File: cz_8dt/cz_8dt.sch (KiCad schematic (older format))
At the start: 638 parts, among them IC1001 74LS09, IC1002 4001, IC1003 4049, IC101 MC4044, IC102 CD4053B, IC103 HD440072, IC104 4069, IC105 HA11720, IC106 74LS221, IC1101 74LS145, IC1102 74LS145, IC1103 74LS145, IC1104 7406, IC1105 74LS26, IC1106 7408, IC1201 7407, IC1202 7406, IC1203 74LS74, IC301 TA7348P, IC302 TA7348P, IC303 TA7347P, IC305 TA7348P, IC401 TA7348P, IC402 TA7348P, IC403 TA7347P, IC404 BA7001, IC404 TA7347P, IC601 X0065CE, IC602 74LS221, IC603 74LS221, IC604 74LS221, IC801 TA7608CP, IC901 74159, IC902 74LS126, IC903 74LS126, IC904 74279, IC905 74279, IC906 74279, IC907 74LS126, IC908 74LS11, IC909 7406, Q1001 Q_NPN_BCE, Q1002 Q_NPN_BCE, Q101 Q_NPN_BCE, Q102 Q_NPN_BCE, Q103 Q_NPN_BCE, Q104 Q_NPN_BCE, Q105 Q_NPN_BCE, Q106 Q_NPN_BCE, Q107 Q_NPN_BCE, Q108 Q_NPN_BCE, Q109 Q_NPN_BCE, Q1099 Q_NPN_BCE, Q1101 Q_PNP_BCE, Q1102 Q_NPN_BCE, Q1103 Q_NPN_BCE, Q1104 Q_PNP_BCE, Q1105 Q_NPN_BCE, Q1106 Q_NPN_BCE, Q1107 Q_PNP_BCE, Q1108 Q_NPN_BCE, Q1109 Q_NPN_BCE, Q1110 Q_NPN_BCE, Q1111 Q_NPN_BCE, Q1112 Q_NPN_BCE, Q1113 Q_NPN_BCE, Q1114 Q_NPN_BCE, Q1115 Q_NPN_BCE, Q112 Q_NPN_BCE, Q301 Q_NPN_BCE, Q303 Q_NPN_BCE, Q304 Q_NPN_BCE, Q316 Q_NPN_BCE, Q401 Q_NPN_BCE, Q402 Q_PNP_BCE, Q403 Q_NPN_BCE, Q413 Q_NPN_BCE, Q414 Q_NPN_BCE, Q415 Q_NPN_BCE, Q416 Q_NPN_BCE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

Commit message: transistor types added and corrections...
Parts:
- removed Q1112, Q1113, Q1114, Q413, Q?: Q_NPN_BCE, symbol Device:Q_NPN_BCE
- added Q111: A105, symbol Device:Q_PNP_BCE
- added Q1112, Q1113, Q1114, Q413: A1015, symbol Device:Q_PNP_BCE
- Q1001, Q1002, Q101, Q102, Q103, Q105, Q109, Q1099, Q1102, Q1103, Q1105, Q1106, Q1108, Q1109, Q1110, Q1111, Q1115, Q112, Q301, Q303, Q304, Q316, Q401, Q403, Q414, Q415, Q416, Q601, Q602, Q603, Q604, Q605: value Q_NPN_BCE -> C1815
- Q104, Q107: value Q_NPN_BCE -> C460
- Q106, Q108: value Q_NPN_BCE -> A454
- Q1101, Q1104, Q1107, Q402: value Q_PNP_BCE -> A1015
- Q412: renamed from Q?; value Q_NPN_BCE -> C1815
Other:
- moved on the sheet: C419, C420, C421, C438, C439, C440, C601, C602, C603, C604, C606, C607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

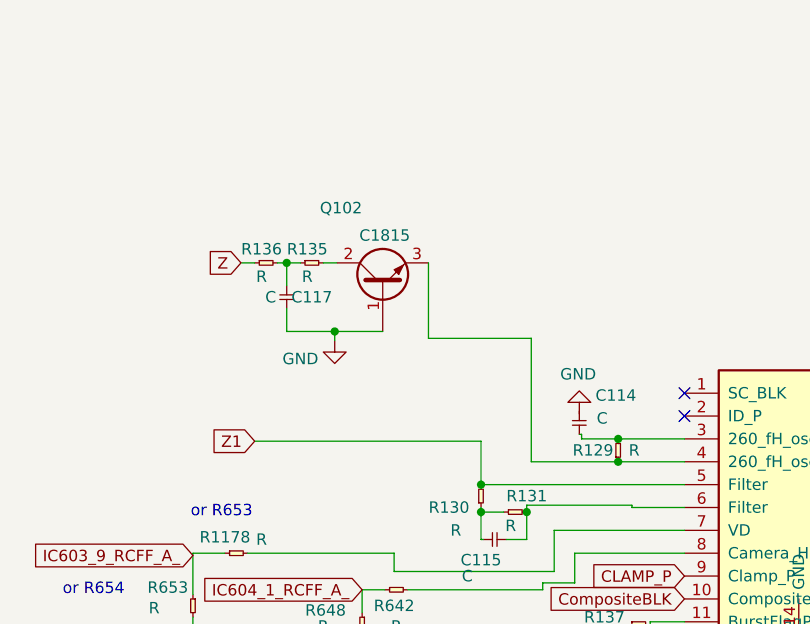
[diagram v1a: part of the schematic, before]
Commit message: changed Q102 to D102 (1SV55 type)
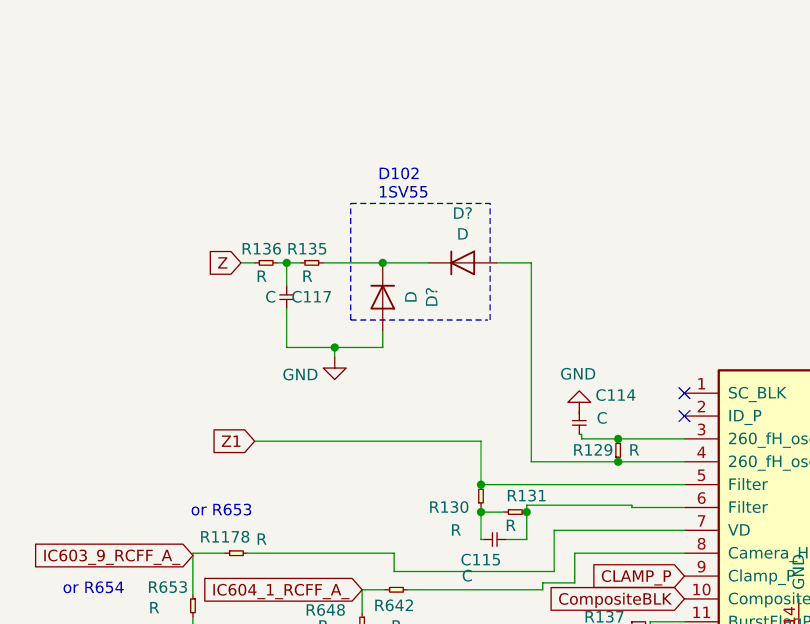
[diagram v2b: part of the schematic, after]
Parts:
- removed Q102: C1815, symbol Device:Q_NPN_BCE
- added D? (x2): D, symbol Device:D
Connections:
- wire segments 2462 -> 2463
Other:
- note added: "D102\n1SV55"
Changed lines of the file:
@@
 L power:GND #PWR?
 U 1 1 668AD11E
-P 15450 6290
-F 0 "#PWR?" H 15450 6040 50  0001 C CNN
-F 1 "GND" H 15300 6210 50  0000 C CNN
-F 2 "" H 15450 6290 50  0001 C CNN
-F 3 "" H 15450 6290 50  0001 C CNN
-	1    15450 6290
+P 15450 6360
+F 0 "#PWR?" H 15450 6110 50  0001 C CNN
+F 1 "GND" H 15300 6280 50  0000 C CNN
+F 2 "" H 15450 6360 50  0001 C CNN
+F 3 "" H 15450 6360 50  0001 C CNN
+	1    15450 6360
 	1    0    0    -1
 $EndComp
@@
 	15100 5950 15040 5950
 Wire Wire Line
-	15400 5950 15460 5950
-$Comp
-L Device:Q_NPN_BCE Q102
-U 1 1 66C5C3E9
-P 15660 6050
-F 0 "Q102" V 16000 6140 50  0000 L CNN
-F 1 "C1815" V 15880 5930 50  0000 L CNN
-F 2 "" H 15860 6150 50  0001 C CNN
-F 3 "~" H 15660 6050 50  0001 C CNN
-	1    15660 6050
-	0    -1   -1   0
-$EndComp
-Wire Wire Line
-	15660 6250 15450 6250
-Wire Wire Line
-	15450 6250 15450 6290
-Wire Wire Line
-	15450 6250 15240 6250
-Wire Wire Line
-	15240 6250 15240 6150
-Connection ~ 15450 6250
+	15450 6320 15450 6360
 Text GLabel 15100 6730 0    50   Input ~ 0
 Z1
@@
 Connection ~ 16290 7040
 Wire Wire Line
-	15860 6280 15860 5950
-Wire Wire Line
-	15860 6280 16310 6280
-Wire Wire Line
 	16750 7010 16750 7020
 Wire Wire Line
@@
 Wire Wire Line
 	16690 6820 16310 6820
-Wire Wire Line
-	16310 6820 16310 6280
 Connection ~ 16690 6820
 Wire Wire Line
@@
 Wire Wire Line
 	16520 16860 16690 16860
+$Comp
+L Device:D D?
+U 1 1 E546E3F8
+P 16010 5950
+F 0 "D?" H 16010 6166 50  0000 C CNN
+F 1 "D" H 16010 6075 50  0000 C CNN
+F 2 "" H 16010 5950 50  0001 C CNN
+F 3 "~" H 16010 5950 50  0001 C CNN
+	1    16010 5950
+	1    0    0    -1
+$EndComp
+$Comp
+L Device:D D?
+U 1 1 E546F3CA
+P 15660 6100
+F 0 "D?" H 15660 6316 50  0000 C CNN
+F 1 "D" H 15660 6225 50  0000 C CNN
+F 2 "" H 15660 6100 50  0001 C CNN
+F 3 "~" H 15660 6100 50  0001 C CNN
+	1    15660 6100
+	0    1    1    0
+$EndComp
+Wire Wire Line
+	15400 5950 15660 5950
+Wire Wire Line
+	15660 5950 15860 5950
+Connection ~ 15660 5950
+Wire Wire Line
+	16160 5950 16310 5950
+Wire Wire Line
+	16310 5950 16310 6820
+Wire Notes Line
+	15520 6200 16120 6200
+Text Notes 15640 5680 0    50   ~ 0
+D102\n1SV55
+Wire Wire Line
+	15660 6250 15660 6320
+Wire Wire Line
+	15660 6320 15450 6320
+Wire Wire Line
+	15450 6320 15240 6320
+Connection ~ 15450 6320
+Wire Wire Line
+	15240 6150 15240 6320
+Wire Notes Line
+	15520 6200 15520 5690
+Wire Notes Line
+	15520 5690 16130 5690
+Wire Notes Line
+	16130 6200 16130 5690
 $EndSCHEMATC

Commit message: updated capa/resistor lists. Added J1/J2/K1/K2
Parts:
- added C342: 100uf/16v, symbol agg-kicad:CP
- added C343, C344, C345: 10uf/16v, symbol agg-kicad:CP
- added C?: 100uf/35V, symbol agg-kicad:CP
- added D303, D305, D306, D307, D308, D309, D310: D, symbol agg-kicad:D
- added D304: 4.7R, symbol agg-kicad:R
- added Q305: A1015, symbol Device:Q_PNP_BCE
- added Q306, Q307, Q308, Q309, Q310, Q311, Q901: C1815, symbol Device:Q_NPN_BCE
- added R1164, R177: R_POT, symbol Device:R_POT
- added R1199, R360: R, symbol agg-kicad:R
- added R358: 10K, symbol agg-kicad:R
- added R359, R361, R363, R365: 3.3K, symbol agg-kicad:R
- added R362, R364, R366: 1K, symbol agg-kicad:R
- added R940: 27R, symbol agg-kicad:R
- added R941: 68R, symbol agg-kicad:R
- added R942: 220R, symbol agg-kicad:R
- added R?: 82R, symbol agg-kicad:R
- renumbered Q1110 to Q110
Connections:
- net labels added: 15V???, RGB21_AUDIO_OUT_L, RGB21_AUDIO_OUT_R, YM_IN, YM_OUT
- wire segments 2463 -> 2557
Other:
- note added: "Audio dc level board ??? (F2868CE)\n\n"
- note added: "COMP video"
- note added: "I-connector:\n------------\nV-position\nH-position\nColor Intensity\nColor tone\nVideo adjustment"
- note added: "Shadow"

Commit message: added power supply schematics
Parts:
- added A: CONN_01x02, symbol agg-kicad:CONN_01x02
- added B: CONN_01x03, symbol agg-kicad:CONN_01x03
- added C701: 104K, symbol agg-kicad:C
- added C702, C703: 103 / 250v, symbol agg-kicad:C
- added C704, C708, C712: 103K, symbol agg-kicad:C
- added C705: 2200uf/35v, symbol agg-kicad:CP
- added C706: 47uf/25v, symbol agg-kicad:CP
- added C707: 100uf/16v, symbol agg-kicad:CP
- added C709: 2200uf/25v, symbol agg-kicad:CP
- added C710: 47uf/16v, symbol agg-kicad:CP
- added C?: 2200uf? 35v ?, symbol agg-kicad:CP
- added D701, D702: D, symbol agg-kicad:D
- added D703: ZENER, symbol agg-kicad:ZENER
- added E: CONN_01x04, symbol agg-kicad:CONN_01x04
- added F701: FUSE, symbol agg-kicad:FUSE
- added IC: L7812, symbol Regulator_Linear:L7812
- added IC702: LM7805, Package_TO_SOT_THT:TO-220-3_Vertical, symbol Regulator_Linear:LM7805_TO220
- added L701: _, symbol Device:Transformer_1P_1S
- added R701: =wire, symbol agg-kicad:R
- added R702: 0.56R, symbol agg-kicad:R
- added R703: 18R, symbol agg-kicad:R
- added R?: 33R-5W, symbol agg-kicad:R
- added R?: 0.5R, symbol agg-kicad:R
- added SW?: SWITCH_SPST, symbol agg-kicad:SWITCH_SPST
- added T?: Transformer_1P_1S, symbol Device:Transformer_1P_1S
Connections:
- net labels added: 15V, AC_100V_1, AC_100V_2, E1, E2, E3, E4
- net labels removed: 15V???
- wire segments 2557 -> 2677
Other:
- note added: "12V\n7.2V\n5V\nGND"
- note added: "<--red wire"
- note added: "Joystick port\nfor external control"
- note added: "POWER SUPPLY"
- note added: "black"
- note added: "black wire ->"
- note added: "brown"
- note added: "brown\n wire\n<--\n"
- note added: "orange"
- note added: "red"
- note added: "to Power\n LED"
- note added: "yellow"
- moved on the sheet: C628, IC1003C, IC1106D, IC901, R916, R917, R918, R919, R924

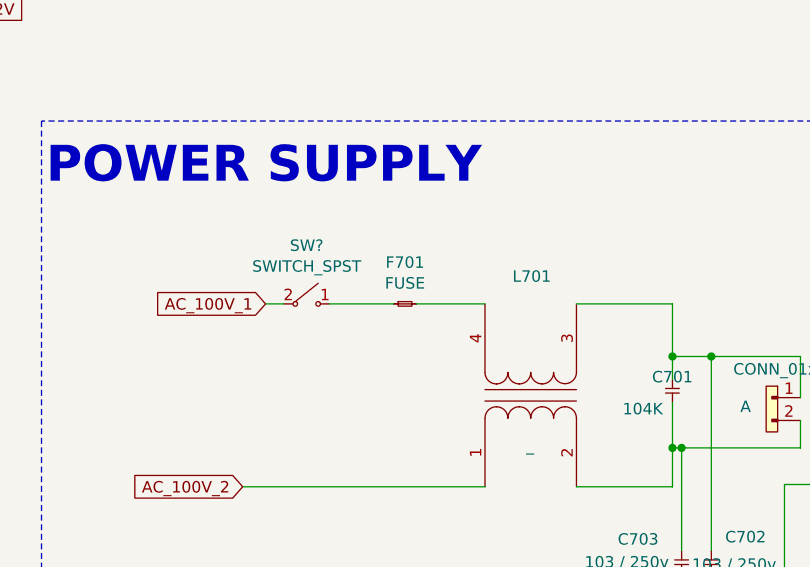
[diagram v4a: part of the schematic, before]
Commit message: updated resistor list
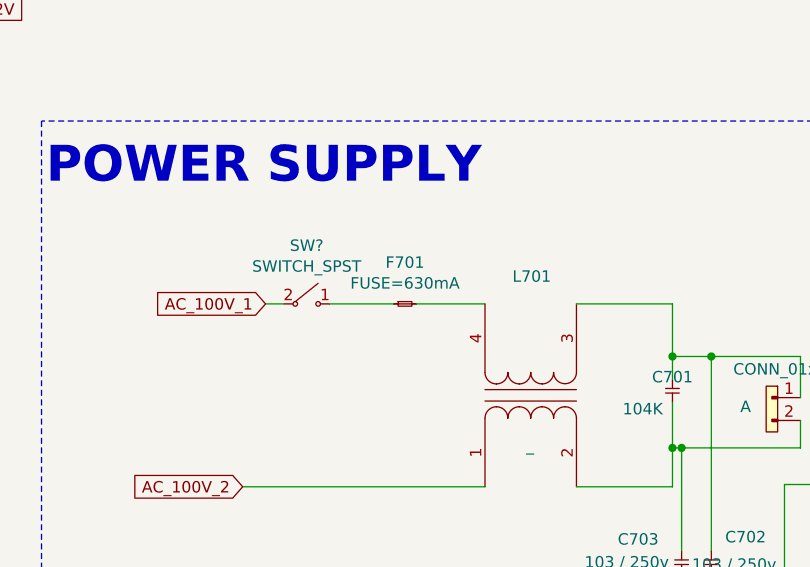
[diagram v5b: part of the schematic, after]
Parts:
- F701: value FUSE -> FUSE=630mA
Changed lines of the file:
@@
 P 12150 2710
 F 0 "F701" H 12200 2891 50  0000 C CNN
-F 1 "FUSE" H 12200 2800 50  0000 C CNN
+F 1 "FUSE=630mA" H 12200 2800 50  0000 C CNN
 F 2 "" H 12205 2770 50  0001 C CNN
 F 3 "" H 12205 2770 50  0001 C CNN

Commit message: add one backpanel pcb
added backpanel pcb that has adjustable resistors, L1-3 and I1-5 are coming here
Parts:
- added C461: 10uf/16v, symbol agg-kicad:CP
- added R460, R462, R463: R_POT, symbol Device:R_POT
- added R461: =wire, symbol agg-kicad:R
- added R645, R646: R_POT_Small, symbol Device:R_POT_Small
- added R?: 12K, symbol agg-kicad:R
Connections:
- wire segments 2677 -> 2716
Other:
- note added: "2nd \nblack"
- note added: "2nd brown"
- note added: "2nd red\nwire"
- note added: "3rd \nblack"
- note added: "3rd brown\nwire"
- note added: "backpanel\nadjustments\n\n"
- note added: "thick\nbrown"
- note added: "white"
- note removed: "black"
- note removed: "brown"
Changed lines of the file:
@@
 	14050 3340 14050 3220
 Text Notes 16760 3080 0    50   ~ 0
-black
+2nd \nblack
 Text Notes 17390 3220 0    50   ~ 0
 red
 Text Notes 17190 3420 0    50   ~ 0
-brown
+2nd brown
 Text Notes 18400 4040 0    59   ~ 0
 12V\n7.2V\n5V\nGND
@@
 P 17740 3800
 F 0 "C706" V 17880 3610 50  0000 L CNN
-F 1 "47uf/25v" V 17740 3520 50  0000 L CNN
+F 1 "47uf/25v" V 17710 3630 50  0000 L CNN
 F 2 "" H 17740 3800 50  0001 C CNN
 F 3 "" H 17740 3800 50  0001 C CNN
@@
 yellow
 Text Notes 17440 3920 0    50   ~ 0
-black
+3rd \nblack
+Text Notes 14930 3330 0    50   ~ 0
+yellow
+Text Notes 15120 2930 0    50   ~ 0
+red
+Text Notes 14960 3430 0    50   ~ 0
+white
+Text Notes 13620 2910 0    50   ~ 0
+thick\nbrown
+Text Notes 13630 3410 0    50   ~ 0
+thick\nbrown
+Text Notes 18480 2830 0    50   ~ 0
+2nd red\nwire
+Text Notes 18610 3150 0    50   ~ 0
+3rd brown\nwire
+$Comp
+L Device:R_POT R462
+U 1 1 CCD520D4
+P 12040 24130
+F 0 "R462" H 11971 24176 50  0000 R CNN
+F 1 "R_POT" H 11971 24085 50  0000 R CNN
+F 2 "" H 12040 24130 50  0001 C CNN
+F 3 "~" H 12040 24130 50  0001 C CNN
+	1    12040 24130
+	1    0    0    -1
+$EndComp
+$Comp
+L Device:R_POT R460
+U 1 1 CCD793F0
+P 12040 25420
+F 0 "R460" H 11971 25466 50  0000 R CNN
+F 1 "R_POT" H 11971 25375 50  0000 R CNN
+F 2 "" H 12040 25420 50  0001 C CNN
+F 3 "~" H 12040 25420 50  0001 C CNN
+	1    12040 25420
+	1    0    0    -1
+$EndComp
+$Comp
+L Device:R_POT R463
+U 1 1 CD5C9FD8
+P 12040 24720
+F 0 "R463" H 11971 24766 50  0000 R CNN
+F 1 "R_POT" H 11971 24675 50  0000 R CNN
+F 2 "" H 12040 24720 50  0001 C CNN
+F 3 "~" H 12040 24720 50  0001 C CNN
+	1    12040 24720
+	1    0    0    -1
+$EndComp
+$Comp
+L Device:R_POT_Small R645
+U 1 1 CEEBD291
+P 10820 24470
+F 0 "R645" H 10761 24516 50  0000 R CNN
+F 1 "R_POT_Small" H 10761 24425 50  0000 R CNN
+F 2 "" H 10820 24470 50  0001 C CNN
+F 3 "~" H 10820 24470 50  0001 C CNN
+	1    10820 24470
+	1    0    0    -1
+$EndComp
+$Comp
+L Device:R_POT_Small R646
+U 1 1 CEEBDA96
+P 10820 24880
+F 0 "R646" H 10761 24926 50  0000 R CNN
+F 1 "R_POT_Small" H 10761 24835 50  0000 R CNN
+F 2 "" H 10820 24880 50  0001 C CNN
+F 3 "~" H 10820 24880 50  0001 C CNN
+	1    10820 24880
+	1    0    0    -1
+$EndComp
+$Comp
+L agg-kicad:CP C461
+U 1 1 CFF6030C
+P 11640 25560
+F 0 "C461" V 11800 25730 50  0000 C CNN
+F 1 "10uf/16v" V 11680 25830 50  0000 C CNN
+F 2 "" H 11640 25560 50  0001 C CNN
+F 3 "" H 11640 25560 50  0001 C CNN
+	1    11640 25560
+	0    -1   -1   0
+$EndComp
+Text GLabel 10080 24250 0    50   Input ~ 0
+L1
+Text GLabel 10090 24640 0    50   Input ~ 0
+L2
+Text GLabel 10090 25000 0    50   Input ~ 0
+L3
+Text GLabel 12730 24640 2    50   Input ~ 0
+I1
+Text GLabel 12240 24130 2    50   Input ~ 0
+I2
+Text GLabel 12300 25420 2    50   Input ~ 0
+I3
+Text GLabel 12280 24720 2    50   Input ~ 0
+I4
+Text GLabel 11450 23910 0    50   Input ~ 0
+I5
+$Comp
+L agg-kicad:R R461
+U 1 1 D290530F
+P 11690 23910
+F 0 "R461" H 11740 24091 50  0000 C CNN
+F 1 "=wire" H 11740 24000 50  0000 C CNN
+F 2 "" H 11690 23910 50  0001 C CNN
+F 3 "" H 11690 23910 50  0001 C CNN
+	1    11690 23910
+	1    0    0    -1
+$EndComp
+Wire Wire Line
+	12040 23980 12040 23910
+Wire Wire Line
+	12040 23910 11790 23910
+Wire Wire Line
+	11690 23910 11640 23910
+Wire Wire Line
+	11640 23910 11640 24570
+Wire Wire Line
+	11640 24570 12040 24570
+Connection ~ 11640 23910
+Wire Wire Line
+	11640 23910 11450 23910
+Wire Wire Line
+	12190 24130 12240 24130
+Wire Wire Line
+	12190 25420 12300 25420
+Wire Wire Line
+	12280 24720 12190 24720
+Wire Wire Line
+	12040 24280 12040 24410
+Wire Wire Line
+	12040 24410 12580 24410
+Wire Wire Line
+	12580 24410 12580 24640
+Wire Wire Line
+	12580 25050 12040 25050
+Wire Wire Line
+	12040 25050 12040 24870
+Wire Wire Line
+	12730 24640 12580 24640
+Connection ~ 12580 24640
+Wire Wire Line
+	12580 24640 12580 25050
+Wire Wire Line
+	12040 25570 12040 25730
+Wire Wire Line
+	12040 25730 12230 25730
+$Comp
+L agg-kicad:R R?
+U 1 1 DD87360A
+P 12230 25730
+F 0 "R?" H 12270 25790 50  0000 C CNN
+F 1 "12K" H 12290 25670 50  0000 C CNN
+F 2 "" H 12230 25730 50  0001 C CNN
+F 3 "" H 12230 25730 50  0001 C CNN
+	1    12230 25730
+	1    0    0    -1
+$EndComp
+Wire Wire Line
+	12330 25730 12580 25730
+Wire Wire Line
+	12580 25730 12580 25050
+Connection ~ 12580 25050
+Wire Wire Line
+	12040 25270 12040 25210
+Wire Wire Line
+	12040 25210 11640 25210
+Wire Wire Line
+	11640 25210 11640 24570
+Connection ~ 11640 24570
+Wire Wire Line
+	11640 25460 11640 25210
+Connection ~ 11640 25210
+Wire Wire Line
+	11640 25560 11640 26000
+Wire Wire Line
+	11640 26000 12580 26000
+Wire Wire Line
+	12580 26000 12580 25730
+Connection ~ 12580 25730
+Wire Wire Line
+	10820 24570 10820 24640
+Wire Wire Line
+	10090 24640 10820 24640
+Connection ~ 10820 24640
+Wire Wire Line
+	10820 24640 10820 24780
+Wire Wire Line
+	10820 24370 10820 24250
+Wire Wire Line
+	10820 24250 10080 24250
+Wire Wire Line
+	10920 24470 10920 24250
+Wire Wire Line
+	10920 24250 10820 24250
+Connection ~ 10820 24250
+Wire Wire Line
+	10920 24880 10920 25070
+Wire Wire Line
+	10920 25070 10820 25070
+Wire Wire Line
+	10090 25000 10820 25000
+Wire Wire Line
+	10820 24980 10820 25000
+Connection ~ 10820 25000
+Wire Wire Line
+	10820 25000 10820 25070
+Wire Notes Line
+	9760 23660 12920 23660
+Wire Notes Line
+	12920 23660 12920 26030
+Wire Notes Line
+	12920 26030 9760 26030
+Wire Notes Line
+	9760 26030 9760 23660
+Text Notes 9850 24100 0    79   ~ 16
+backpanel\nadjustments\n\n
 $EndSCHEMATC

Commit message: added N-connector RGB21 target pins
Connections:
- net labels added: N2
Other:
- note added: "N1\n1\n2\nN2\n1\n2\n3\n4\n5\nN3\n1\n2\nN4\n1\n2\n3\n4\n5"
- note added: "Not a typo!\nRCA input 3 and RGB21 audio input channels are\nswapped connected, so this is clearly a design bug!"
- note added: "RCA"
- note added: "RGB21\nBLUE"
- note added: "RGB21\nCSynch/CompVideo IN"
- note added: "RGB21\nGREEN"
- note added: "RGB21\nL AUDIO IN"
- note added: "RGB21\nL AUDIO OUT"
- note added: "RGB21\nR AUDIO OUT"
- note added: "RGB21\nRED"
- note added: "RGB\nav control input"
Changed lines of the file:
@@
 	8070 15700 8070 15750
 Text GLabel 8320 15700 2    50   Input ~ 0
-N4
+N2
 Wire Wire Line
 	8070 15700 8220 15700
@@
 Text Notes 9850 24100 0    79   ~ 16
 backpanel\nadjustments\n\n
+Text Notes 11360 27950 0    50   ~ 0
+N1\n1\n2\nN2\n1\n2\n3\n4\n5\nN3\n1\n2\nN4\n1\n2\n3\n4\n5
+Text Notes 2940 17570 0    50   ~ 0
+RGB\nav control input
+Text Notes 32210 8300 0    50   ~ 0
+RGB21\nBLUE
+Text Notes 32180 9350 0    50   ~ 0
+RGB21\nRED
+Text Notes 32170 10360 0    50   ~ 0
+RGB21\nGREEN
+Text Notes 8520 15820 0    50   ~ 0
+RGB21\nR AUDIO OUT
+Text Notes 8510 17130 0    50   ~ 0
+RGB21\nL AUDIO OUT
+Text Notes -40  16720 0    50   ~ 0
+RGB21\nCSynch/CompVideo IN
+Text Notes 700  17110 0    50   ~ 0
+RCA
+Text Notes 690  16010 0    50   ~ 0
+RCA
+Text Notes 680  14890 0    50   ~ 0
+RCA
+Text Notes 3420 19810 0    50   ~ 0
+RGB21\nL AUDIO IN
+Text Notes 240  19200 0    50   ~ 0
+RGB21\nL AUDIO IN
+Text Notes -1070 19830 0    50   ~ 0
+Not a typo!\nRCA input 3 and RGB21 audio input channels are\nswapped connected, so this is clearly a design bug!
 $EndSCHEMATC

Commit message: added H-connector pins
added H-connector pins and external DSUB joystick port pinout command mapping
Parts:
- added H_: CONN_01x12, symbol agg-kicad:CONN_01x12
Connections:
- net labels added: DSUB_PIN6, DSUB_PIN7, DSUB_PIN8, DSUB_PIN9
- net labels removed: H1
- wire segments 2716 -> 2724
- no-connect marks 42 -> 47
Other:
- note added: "Buttons"
- note added: "External control pins:\n4-3-2-1\n0000 -\n0001 rec-out\n0010 mon-3\n0011 mon-2\n0100 mon-1\n0101 Vin-3\n0110 Vin-2\n0111 Vin-1\n1000 Video\n1001 SuperImpose\n1010 Computer\n1011 Reset Teloper\n1100 Set Teloper"
- note added: "Rec-out\nMon-3\nMon-2\nMon-1\nVin-3\nVin-2\nVin-1\nVideo\nSuperImpose\nComputer\nTeloper"
- note added: "When pin 5 put to ground"
- note added: "no wire"
- note removed: "---> IC901 pin13 ????"
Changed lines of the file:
@@
 	13050 12330 13300 12330
 Wire Wire Line
-	13300 12330 13300 14010
+	13300 12330 13300 13850
 Wire Wire Line
 	12040 14010 13300 14010
@@
 Wire Wire Line
 	11650 10180 11600 10180
-Text Notes 13290 14000 0    79   ~ 16
----> IC901 pin13  ????
 Text GLabel 10900 9830 2    50   Input ~ 0
 J18
@@
 Wire Wire Line
 	8060 9820 8160 9820
-Text GLabel 3310 1170 2    50   Input ~ 0
-H1
 Text GLabel 3310 1270 2    50   Input ~ 0
 H2
@@
 Wire Wire Line
 	1710 930  1820 930
-Text GLabel 13310 14050 2    50   Input ~ 0
+Text GLabel 13450 13850 2    50   Input ~ 0
 IC901_~S11
 Text Notes 4210 12130 0    50   ~ 0
@@
 Text Notes -1070 19830 0    50   ~ 0
 Not a typo!\nRCA input 3 and RGB21 audio input channels are\nswapped connected, so this is clearly a design bug!
+$Comp
+L agg-kicad:CONN_01x12 H_
+U 1 1 EFB01F8B
+P 5230 890
+F 0 "H_" H 5263 1105 50  0000 C CNN
+F 1 "CONN_01x12" H 5263 1014 50  0000 C CNN
+F 2 "" H 5230 890 50  0001 C CNN
+F 3 "" H 5230 890 50  0001 C CNN
+	1    5230 890
+	1    0    0    -1
+$EndComp
+Text GLabel 5330 990  2    50   Input ~ 0
+H2
+Text GLabel 5330 1090 2    50   Input ~ 0
+H3
+Text GLabel 5330 1190 2    50   Input ~ 0
+H4
+Text GLabel 5330 1290 2    50   Input ~ 0
+H5
+Text GLabel 5330 1390 2    50   Input ~ 0
+H6
+Text GLabel 5330 1490 2    50   Input ~ 0
+H7
+Text GLabel 5330 1590 2    50   Input ~ 0
+H8
+Text GLabel 5330 1690 2    50   Input ~ 0
+H9
+Text GLabel 5330 1790 2    50   Input ~ 0
+H10
+Text GLabel 5330 1890 2    50   Input ~ 0
+H11
+Text GLabel 5330 1990 2    50   Input ~ 0
+H12
+Wire Wire Line
+	5330 890  5670 890
+NoConn ~ 5670 890
+Text Notes 5730 920  0    50   ~ 0
+no wire
+Text Notes 5530 2040 0    63   ~ 0
+Rec-out\nMon-3\nMon-2\nMon-1\nVin-3\nVin-2\nVin-1\nVideo\nSuperImpose\nComputer\nTeloper
+Text Notes 5480 740  0    98   ~ 20
+Buttons
+Text GLabel 1350 2220 0    50   Input ~ 0
+DSUB_PIN6
+Text GLabel 1350 2360 0    50   Input ~ 0
+DSUB_PIN7
+Text GLabel 1350 2480 0    50   Input ~ 0
+DSUB_PIN8
+Text GLabel 1350 2600 0    50   Input ~ 0
+DSUB_PIN9
+$Comp
+L power:GND #PWR?
+U 1 1 F7306C72
+P 1610 2510
+F 0 "#PWR?" H 1610 2260 50  0001 C CNN
+F 1 "GND" H 1615 2337 50  0000 C CNN
+F 2 "" H 1610 2510 50  0001 C CNN
+F 3 "" H 1610 2510 50  0001 C CNN
+	1    1610 2510
+	1    0    0    -1
+$EndComp
+Wire Wire Line
+	1610 2480 1350 2480
+Wire Wire Line
+	1610 2480 1610 2510
+NoConn ~ 1420 2600
+NoConn ~ 1420 2360
+Wire Wire Line
+	1350 2360 1420 2360
+Wire Wire Line
+	1350 2600 1420 2600
+NoConn ~ 1430 2220
+Wire Wire Line
+	1350 2220 1430 2220
+NoConn ~ 3310 1170
+Wire Wire Line
+	13450 13850 13300 13850
+Connection ~ 13300 13850
+Wire Wire Line
+	13300 13850 13300 14010
+Text Notes 3820 1930 0    50   ~ 0
+External control pins:\n4-3-2-1\n0000 -\n0001 rec-out\n0010 mon-3\n0011 mon-2\n0100 mon-1\n0101 Vin-3\n0110 Vin-2\n0111 Vin-1\n1000 Video\n1001 SuperImpose\n1010 Computer\n1011 Reset Teloper\n1100 Set Teloper
+Text Notes 3800 700  0    50   ~ 0
+When pin 5 put to ground
 $EndSCHEMATC
